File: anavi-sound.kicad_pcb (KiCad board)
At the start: 2 copper layers, 65 x 30 mm, 27 parts, among them Q1 IRF8721PBF-1, Q2 IRF8721PBF-1, Q3 IRF8721PBF-1, U1 CAT24C32WI-GT3

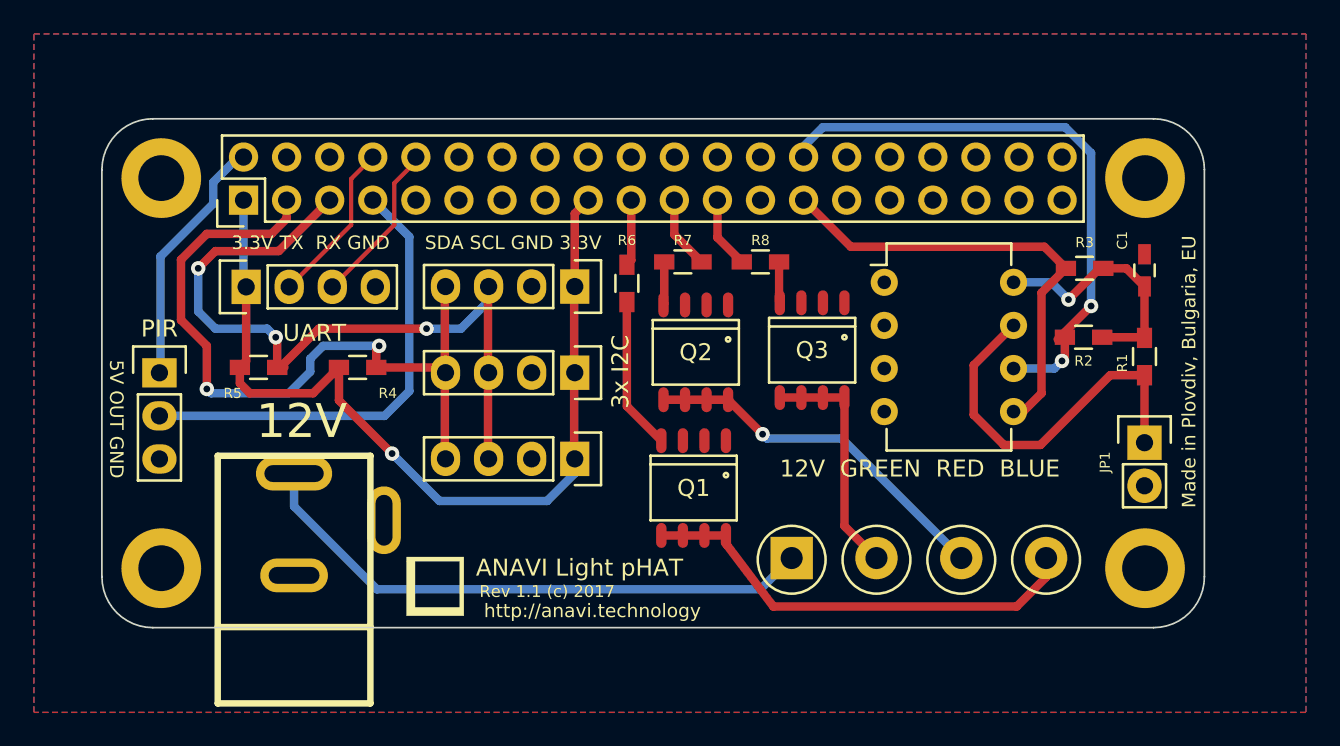
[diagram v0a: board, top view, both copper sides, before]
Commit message: anavi-sound.kicad_pcb: Cleanup
Signed-off-by: Leon Anavi <leon@anavi.org>
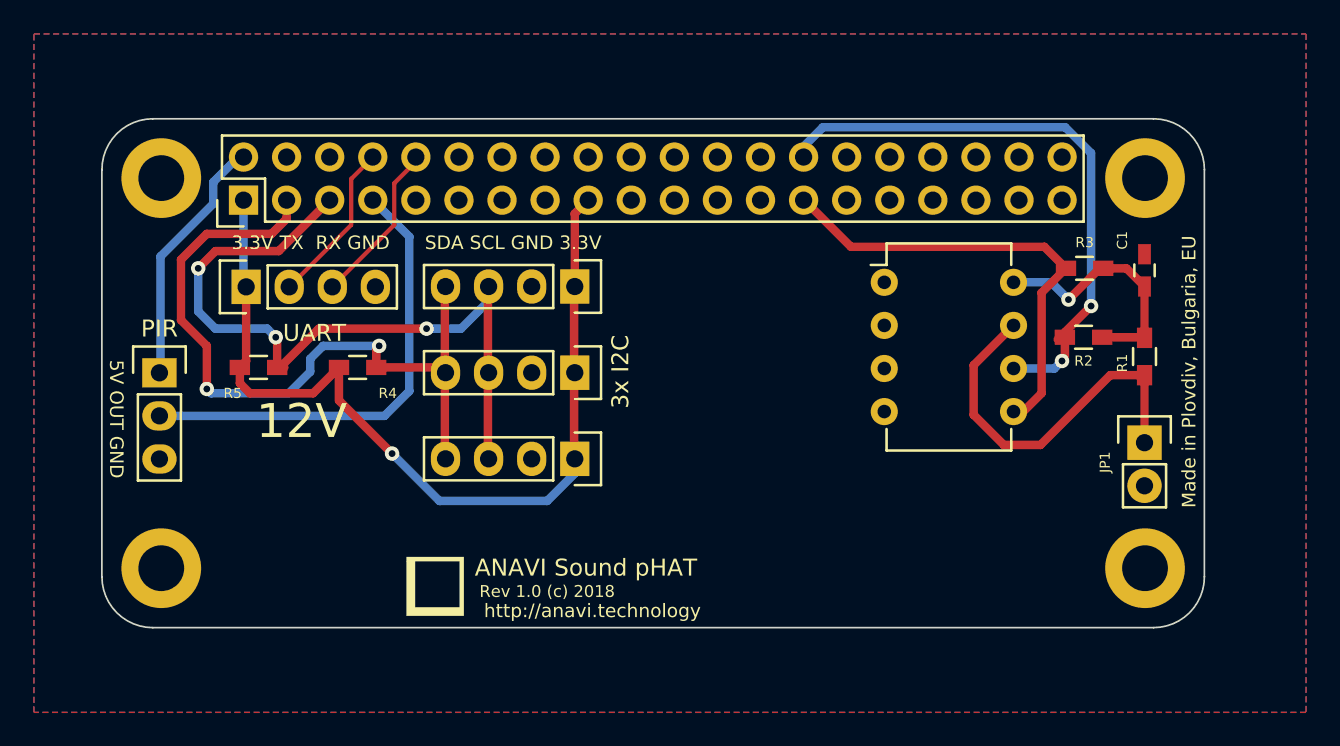
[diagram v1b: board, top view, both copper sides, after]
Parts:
- removed DC1: dc_jack, w_conn_misc:dc_socket
- removed Q1, Q2, Q3: IRF8721PBF-1, SO-8
- removed R6, R7, R8: 220R, Resistors_SMD:R_0603_HandSoldering
- removed RGB1: Screw_Terminal_1x04, myfootprint:TerminalBlock_4PIN
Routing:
- net Net-(DC1-Pad3): track 35.5 -> 0.00 mm
- net Net-(Q1-Pad5): track 27.7 -> 0.00 mm
- net Net-(Q2-Pad5): track 21.8 -> 0.00 mm, vias 1 -> 0
- net Net-(Q3-Pad5): track 14.2 -> 0.00 mm
- net Net-(Q1-Pad4): track 9.01 -> 0.00 mm
- net Net-(R7-Pad2): track 4.30 -> 0.00 mm
- net Net-(R8-Pad2): track 4.23 -> 0.00 mm
- net Net-(R6-Pad2): track 3.92 -> 0.00 mm
- net Net-(Q2-Pad4): track 2.56 -> 0.00 mm
- net Net-(Q3-Pad4): track 2.43 -> 0.00 mm
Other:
- board text added: "ANAVI Sound pHAT"
- board text added: "Rev 1.0 (c) 2018"
- board text removed: "100R"
- board text removed: "12V GREEN RED BLUE"
- board text removed: "ANAVI Light pHAT"
- board text removed: "IRF8721"
- board text removed: "Rev 1.1 (c) 2017"

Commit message: MAX98357A routing
Update footprint and routing.

Signed-off-by: Leon Anavi <leon@anavi.org>
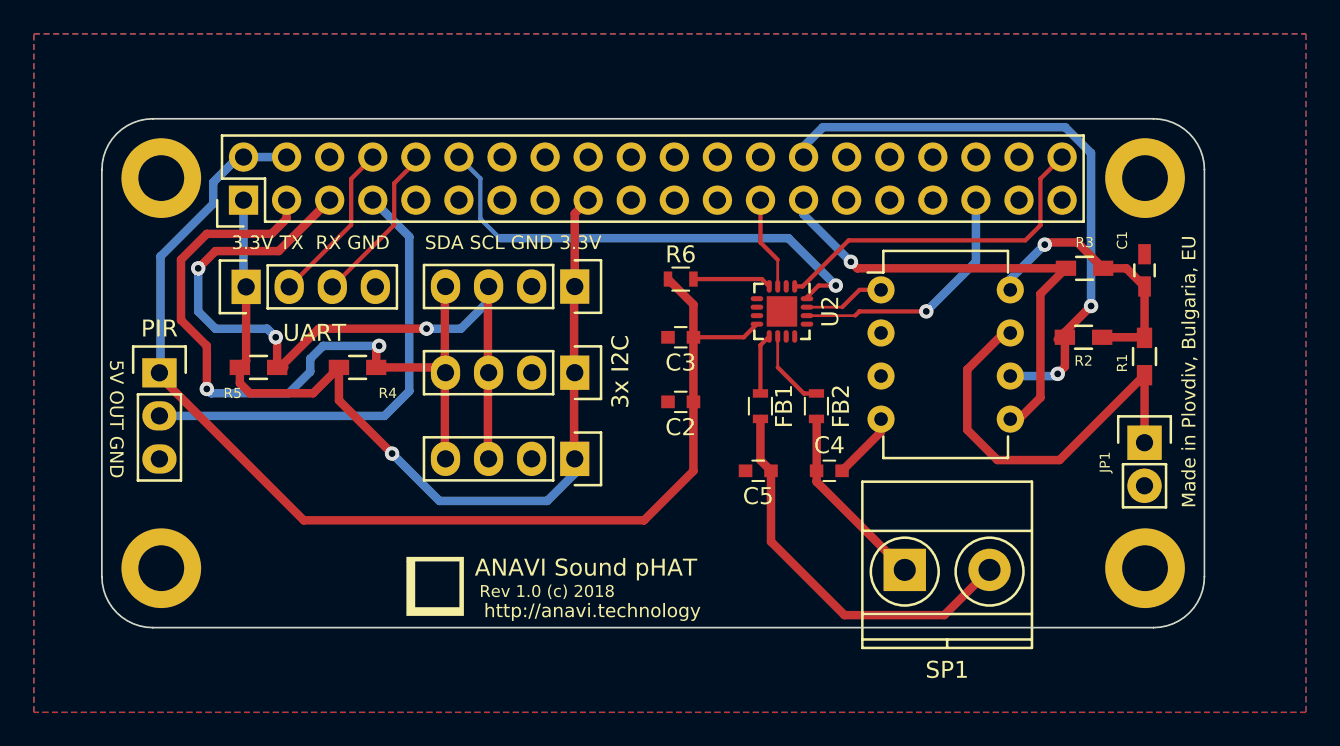
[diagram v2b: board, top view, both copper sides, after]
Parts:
- added C2: 10uF, Capacitors_SMD:C_0603, F.Cu at (182.6, 91.7)
- added C3: 0.1uF, Capacitors_SMD:C_0603, F.Cu at (182.6, 87.9)
- added C4: 220pF, Capacitors_SMD:C_0603, F.Cu at (191.4, 95.8)
- added C5: 220pF, Capacitors_SMD:C_0603, F.Cu at (187.2, 95.8)
- added FB1: 1k, Resistors_SMD:R_0603, F.Cu at (187.3, 91.9)
- added FB2: 1k, Resistors_SMD:R_0603, F.Cu at (190.6, 91.9)
- added R6: 1M, Resistors_SMD:R_0603, F.Cu at (182.6, 84.5)
- added SP1: Screw_Terminal_1x02, Terminal_Blocks:TerminalBlock_Pheonix_MKDS1.5-2pol, F.Cu at (195.8, 101.6)
- added U2: MAX98357, Housings_DFN_QFN:QFN-16-1EP_3x3mm_Pitch0.5mm, F.Cu at (188.6, 86.4)
- moved U1 0.48 mm to (194.4, 85.1)
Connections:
- RASP_CONN1 pad 12: (no net) -> /BCLK
- RASP_CONN1 pad 19: Net-(R6-Pad2) -> (no net)
- RASP_CONN1 pad 21: Net-(R7-Pad2) -> (no net)
- RASP_CONN1 pad 23: Net-(R8-Pad2) -> (no net)
- RASP_CONN1 pad 35: (no net) -> /LRCLK
- RASP_CONN1 pad 40: (no net) -> /DIN
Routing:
- net +5V: track 15.1 -> 70.1 mm
- net /BCLK: track 0.00 -> 28.9 mm, vias 0 -> 1
- net Net-(C5-Pad1): track 0.00 -> 24.1 mm
- net /DIN: track 0.00 -> 20.5 mm
- net /LRCLK: track 0.00 -> 15.3 mm, vias 0 -> 1
- net GND: track 0.00 -> 14.4 mm
- net Net-(C4-Pad1): track 0.00 -> 11.1 mm
- net Net-(FB2-Pad1): track 0.00 -> 4.98 mm
- net Net-(R6-Pad2): track 0.00 -> 4.72 mm
- net Net-(FB1-Pad2): track 0.00 -> 3.58 mm
- net Net-(R3-Pad2): track 27.6 -> 29.2 mm, vias 0 -> 1
- net Net-(JP1-Pad1): track 23.1 -> 24.6 mm
- net +3V3: track 69.7 -> 71.1 mm
- net Net-(R2-Pad2): track 35.4 -> 36.1 mm
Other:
- net class amp added: clearance 0.254, trace_width 0.2, via_dia 0.85, via_drill 0.4
- rule trace_min: 0.25 -> 0.16
- board text removed: "12V"
